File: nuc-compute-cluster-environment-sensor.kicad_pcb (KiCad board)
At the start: 4 copper layers, 112 parts, among them J1 USB4105-GF-A, J2 SM04B-SRSS-TB-LF-SN, J3 SM04B-SRSS-TB-LF-SN, U1 FT4232H-56Q, U2 AP7370-33SA-7, U3 STM32G474CET6, U4 MB85RC1MTPNF-G, U5 SHT45, U6 BME280, Y1 ABM3B-12.000MHZ-B2-T, Y2 ECS-_327-12_5-34B-TR, Y3 ABM3B-8.000MHZ-10-1-U-T

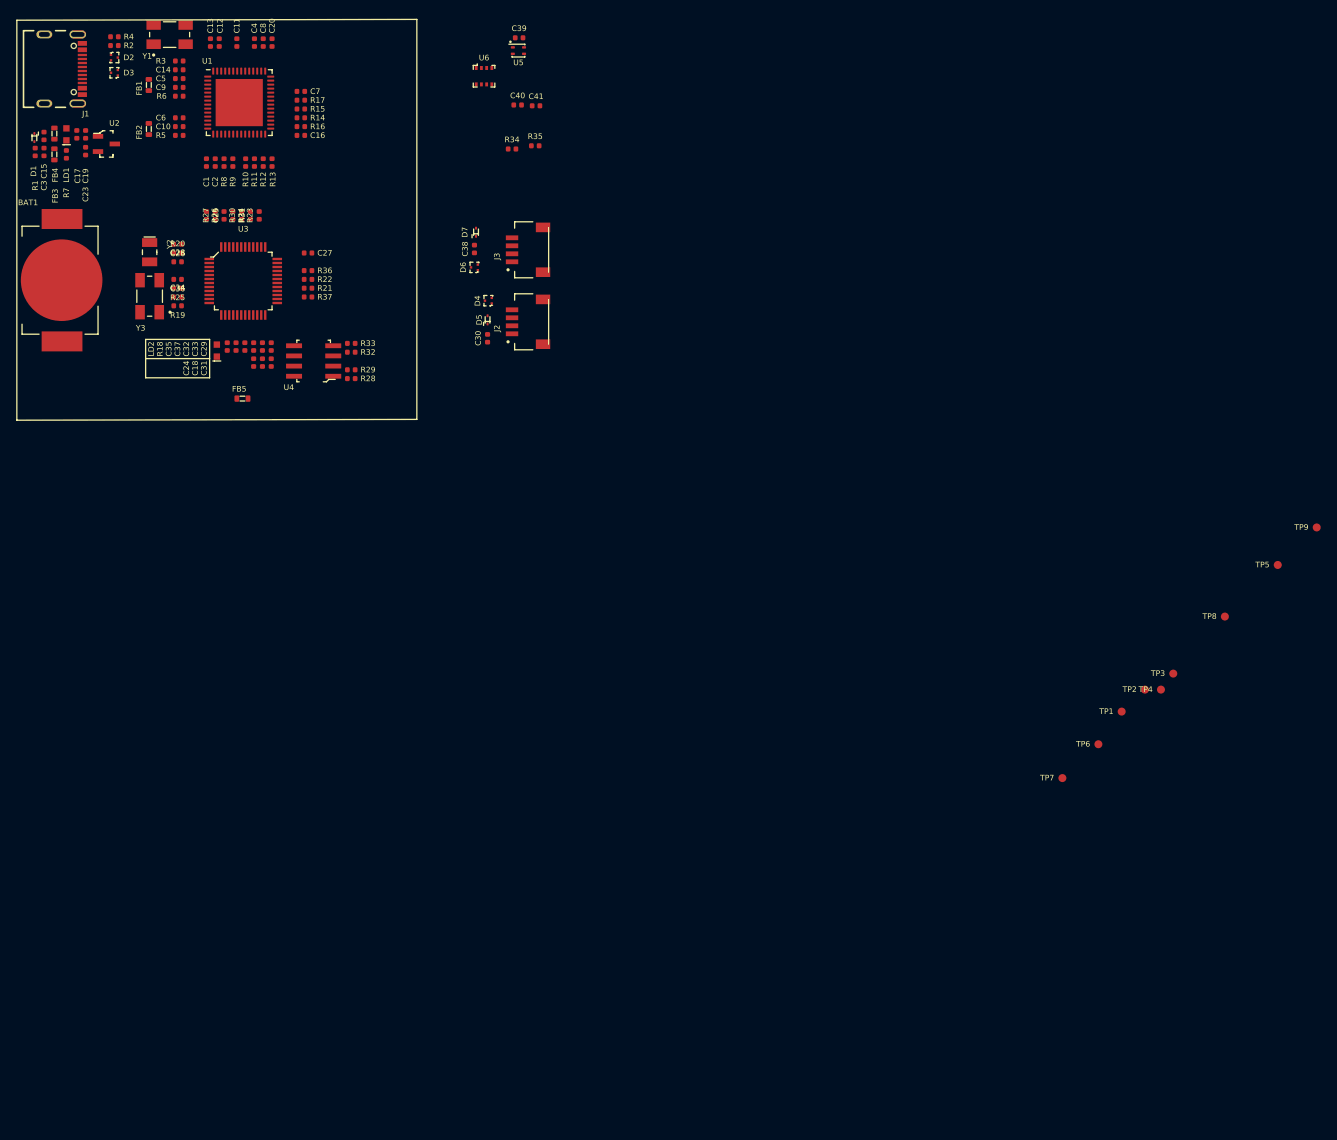
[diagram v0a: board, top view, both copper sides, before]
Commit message: Started to route signals to closest passive components to seek for possible placement optimization
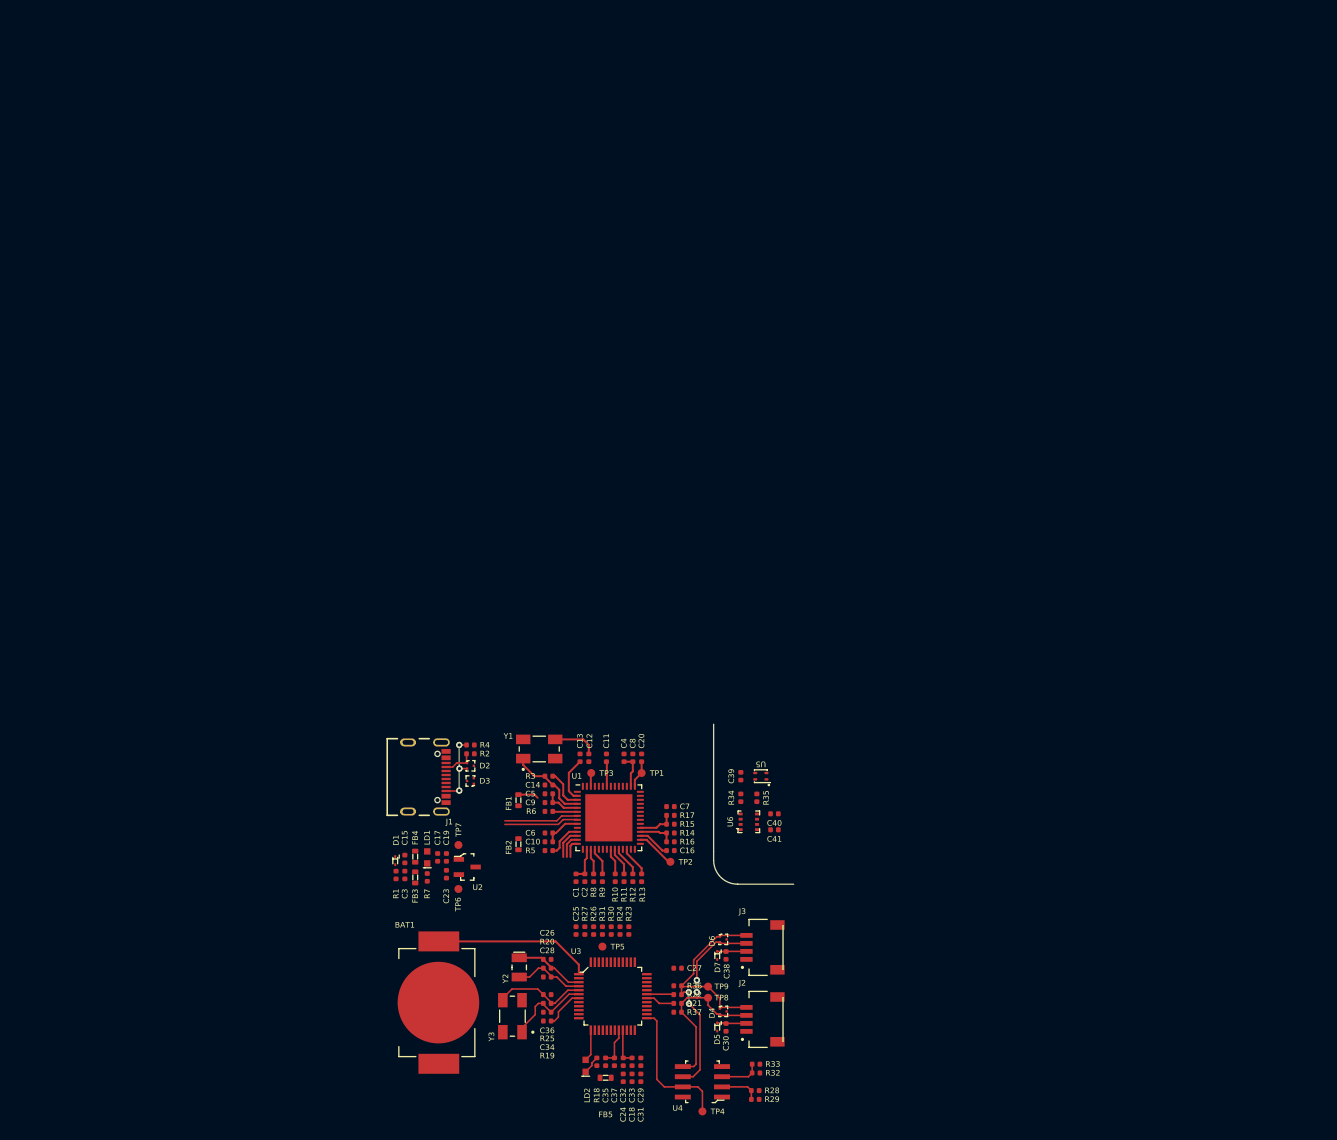
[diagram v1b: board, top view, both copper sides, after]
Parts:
- moved R29 104.2 mm to (115.3, 147.9)
- moved R32 103.3 mm to (115.4, 144.6)
- moved R33 103.3 mm to (115.4, 143.5)
- moved U4 102.4 mm to (108.7, 145.7)
- moved R28 102.3 mm to (115.3, 146.8)
- moved BAT1 101.8 mm to (75.7, 135.8)
- moved C17 101.0 mm to (75.6, 117.7)
- moved C19 101.0 mm to (76.7, 117.7)
- moved FB3 101.0 mm to (72.8, 120.2)
- moved FB4 101.0 mm to (72.8, 117.6)
- moved LD1 101.0 mm to (74.3, 117.7)
- moved R7 101.0 mm to (74.3, 120.2)
- moved C15 101.0 mm to (71.5, 117.8)
- moved C23 101.0 mm to (76.7, 119.8)
- moved C3 101.0 mm to (71.5, 119.8)
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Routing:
- net I2C_1_SCL: track 0.00 -> 36.8 mm, vias 0 -> 2
- net I2C_1_SDA: track 0.00 -> 31.8 mm, vias 0 -> 2
- net Net-(BAT1-PadP): track 0.00 -> 19.9 mm
- net +3V3: track 0.00 -> 19.0 mm
- net /FRAM_WP: track 0.00 -> 17.5 mm
- net /FTDI_+1V8: track 0.00 -> 13.0 mm
- net Net-(C36-Pad2): track 0.00 -> 11.7 mm
- net Net-(C34-Pad2): track 0.00 -> 11.0 mm
- net Net-(C12-Pad2): track 0.00 -> 10.7 mm
- net Net-(C14-Pad2): track 0.00 -> 10.3 mm
- net /USB_D_N: track 0.00 -> 9.32 mm
- net /USB_D_P: track 0.00 -> 9.32 mm
- net /USB_CC2: track 0.00 -> 9.25 mm, vias 0 -> 3
- net Net-(C28-Pad2): track 0.00 -> 8.92 mm
- net Net-(C26-Pad2): track 0.00 -> 8.79 mm
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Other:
- board outline added: 10 x 20 mm

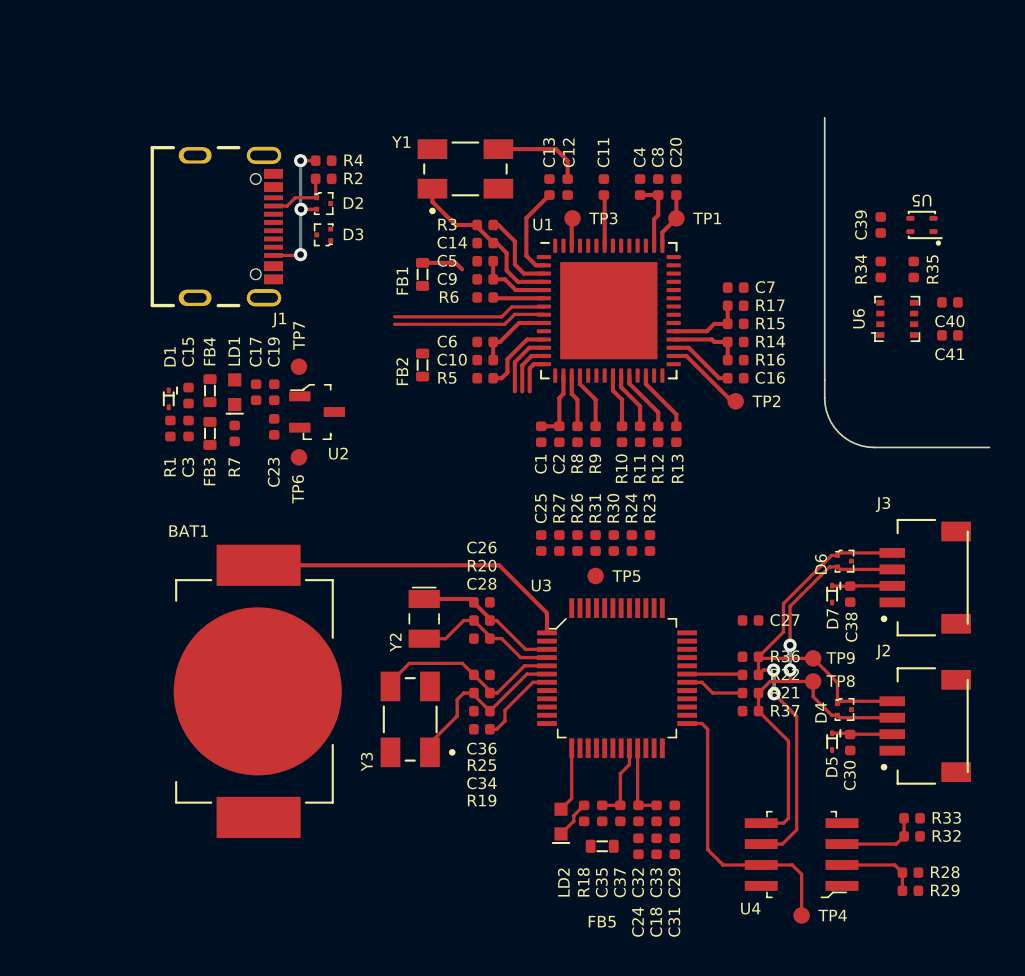
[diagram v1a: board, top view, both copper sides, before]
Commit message: Another iteration of component placements, initial routing of signals
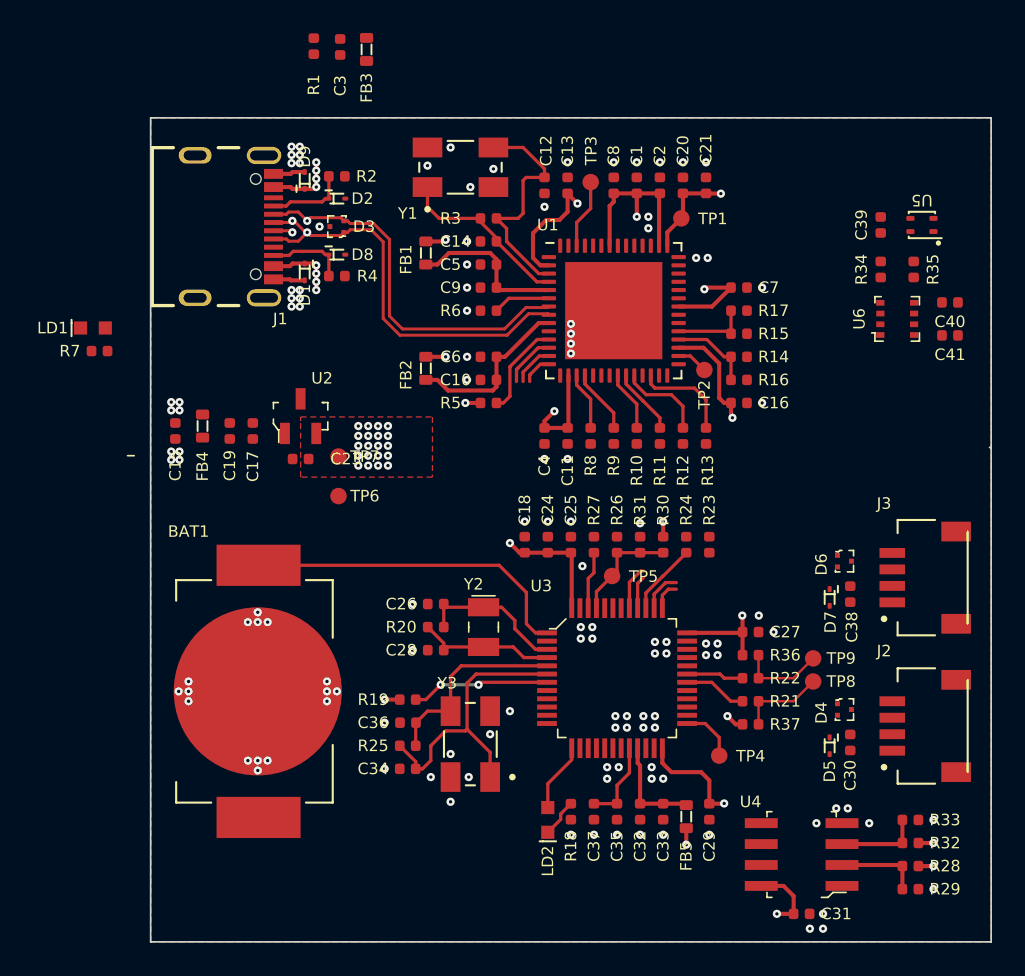
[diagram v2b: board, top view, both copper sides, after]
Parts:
- added C21: C_4u7_0402, antmicro-footprints:0402-cap, F.Cu at (102.9, 105.1)
- added D8: ESD9X5.0ST5G, antmicro-footprints:SOD-923, F.Cu at (80.5, 109.3)
- added D9: ESD9X5.0ST5G, antmicro-footprints:SOD-923, F.Cu at (78.5, 104.8)
- D2: value TPD2E009 -> ESD9X5.0ST5G; footprint antmicro-footprints:SOT-723 -> antmicro-footprints:SOD-923
- moved FB3 25.2 mm to (82.3, 96.8)
- moved C3 24.9 mm to (80.7, 96.7)
- moved R1 24.8 mm to (79.1, 96.7)
- moved C18 20.0 mm to (91.9, 126.9)
- moved C24 19.1 mm to (93.3, 126.9)
- moved C2 16.3 mm to (100.1, 105.1), turned to 90 degrees
- moved C1 16.2 mm to (98.7, 105.1), turned to 90 degrees
- moved C4 16.2 mm to (93.1, 120.3), turned to -90 degrees
- moved C11 15.3 mm to (94.5, 120.3), turned to -90 degrees
- moved D1 11.3 mm to (78.5, 110.3)
- moved TP4 10.9 mm to (103.7, 139.7)
- moved R7 9.60 mm to (66.1, 115.2), turned to 180 degrees
- moved LD1 9.44 mm to (65.7, 113.8), turned to 0 degrees
- moved C31 8.72 mm to (108.7, 149.3), turned to 180 degrees
- moved TP7 8.21 mm to (80.6, 124.0)
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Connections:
- D2 pad 2: /USB_CC2 -> GND
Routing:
- net +3V3: track 19.0 -> 54.9 mm, vias 0 -> 36
- net I2C_1_SCL: track 36.8 -> 5.21 mm, vias 2 -> 0
- net I2C_1_SDA: track 31.8 -> 5.21 mm, vias 2 -> 0
- net /USB_D_P: track 9.32 -> 25.5 mm, vias 0 -> 2
- net /USB_D_N: track 9.32 -> 25.5 mm, vias 0 -> 2
- net /FRAM_WP: track 17.5 -> 3.40 mm
- net /VBUS: track 0.00 -> 8.39 mm, vias 0 -> 12
- net Net-(C34-Pad2): track 11.0 -> 17.8 mm
- net /FTDI_+1V8: track 13.0 -> 19.9 mm, vias 0 -> 3
- net Net-(R26-Pad1): track 0.00 -> 6.68 mm
- net /FTDI_VPLL: track 4.65 -> 10.5 mm
- net /USB_CC2: track 9.25 -> 4.83 mm, vias 3 -> 0
- net Net-(R23-Pad2): track 0.00 -> 4.39 mm
- net GND: track 0.00 -> 3.86 mm, vias 0 -> 120
- net Net-(C12-Pad2): track 10.7 -> 14.3 mm
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- added copper zone on F.Cu, net +3V3
- added copper zone on In2.Cu, net +3V3
- added copper zone on In2.Cu, net /FTDI_+1V8
- added copper zone on In2.Cu, net /VBUS
- added copper zone on B.Cu, net GND
- added copper zone on F.Cu, net GND
- added copper zone on In1.Cu, net GND
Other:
- board size 10 x 20 mm -> 51 x 50 mm

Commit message: Added mounting holes and changed PCB size to 50x30mm
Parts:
- added MP1: PCB_Mount_Hole_2.7mm_M2.5_pad, antmicro-footprints:mounting-hole-2.7mm-M2.5-Pad, F.Cu at (164.0, 114.0)
- added MP2: PCB_Mount_Hole_2.7mm_M2.5_pad, antmicro-footprints:mounting-hole-2.7mm-M2.5-Pad, F.Cu at (164.0, 136.0)
- added MP3: PCB_Mount_Hole_2.7mm_M2.5_pad, antmicro-footprints:mounting-hole-2.7mm-M2.5-Pad, F.Cu at (194.0, 114.0)
- added MP4: PCB_Mount_Hole_2.7mm_M2.5_pad, antmicro-footprints:mounting-hole-2.7mm-M2.5-Pad, F.Cu at (200.0, 136.0)
- moved C27 166.0 mm to (271.1, 145.2)
- moved C29 166.0 mm to (268.6, 156.1)
- moved C37 166.0 mm to (261.6, 156.1)
- moved R21 166.0 mm to (271.1, 149.4)
- moved R22 166.0 mm to (271.1, 148.0)
- moved R23 166.0 mm to (268.6, 139.9)
- moved R27 166.0 mm to (261.6, 139.9)
- moved R36 166.0 mm to (271.1, 146.6)
- moved R37 166.0 mm to (271.1, 150.8)
- moved C24 166.0 mm to (258.8, 139.9)
- moved C25 166.0 mm to (260.2, 139.9)
- moved C26 166.0 mm to (252.0, 143.5)
- moved C28 166.0 mm to (252.0, 146.3)
- moved C33 166.0 mm to (265.8, 156.1)
- moved C34 166.0 mm to (250.3, 153.5)
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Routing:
- net Net-(BAT1-PadP): track 20.3 -> 0.70 mm
- net /USB_D_N: track 25.5 -> 7.62 mm
- net /USB_D_P: track 25.5 -> 7.62 mm
- net GND: vias 120 -> 102
- removed copper zone on F.Cu, net +3V3
- removed copper zone on In2.Cu, net +3V3
- removed copper zone on In2.Cu, net /FTDI_+1V8
- removed copper zone on In2.Cu, net /VBUS
- removed copper zone on B.Cu, net GND
- removed copper zone on F.Cu, net GND
- removed copper zone on In1.Cu, net GND
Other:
- board size 51 x 50 mm -> 50 x 30 mm

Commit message: New component placement, FTDI and related passive components moved to bottom layer
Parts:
- BAT1, C1, C10, C11, C12, C13, C14, C16, C2, C20, C21, C30, C38, C4, C5, C6, C7, C8, C9, D4, D5, D6, D7, FB1, FB2, J2, J3, R10, R11, R12, R13, R14, R15, R16, R17, R3, R5, R6, R8, R9, TP1, TP2, TP3, U1, Y1: moved to B.Cu
- moved C21 95.9 mm to (183.7, 136.4), turned to -90 degrees
- moved C20 95.7 mm to (182.6, 136.4), turned to -90 degrees
- moved C2 95.5 mm to (181.5, 136.4), turned to -90 degrees
- moved C1 95.3 mm to (180.4, 136.4), turned to -90 degrees
- moved C8 95.1 mm to (179.3, 136.4), turned to -90 degrees
- moved C14 95.0 mm to (167.8, 136.3), turned to 90 degrees
- moved Y1 94.9 mm to (171.9, 136.5), turned to -90 degrees
- moved TP3 94.6 mm to (177.2, 134.9), turned to 90 degrees
- moved C13 94.1 mm to (178.2, 136.4), turned to -90 degrees
- moved C12 93.9 mm to (177.1, 136.4)
- moved TP1 92.2 mm to (185.0, 135.9)
- moved R3 90.9 mm to (176.0, 136.4), turned to -90 degrees
- moved C5 88.2 mm to (173.1, 133.4)
- moved FB1 87.6 mm to (170.8, 133.1), turned to 0 degrees
- moved C7 86.9 mm to (186.5, 131.3)
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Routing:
- net +3V3: track 54.9 -> 23.6 mm, vias 36 -> 2
- net /USB_D_N: track 7.62 -> 20.1 mm, vias 2 -> 3
- net /USB_D_P: track 7.62 -> 19.5 mm, vias 2 -> 3
- net Net-(C34-Pad2): track 17.8 -> 7.36 mm
- net NRST: track 8.40 -> 0.00 mm, vias 2 -> 0
- net /FTDI_+1V8: track 19.9 -> 12.2 mm
- net Net-(C14-Pad2): track 10.7 -> 3.86 mm
- net Net-(C12-Pad2): track 14.3 -> 7.69 mm
- net Net-(R32-Pad1): track 5.09 -> 0.09 mm
- net Net-(R28-Pad1): track 5.09 -> 0.09 mm
- net I2C_1_SDA: track 5.21 -> 1.10 mm
- net I2C_1_SCL: track 5.21 -> 1.10 mm
- net /FTDI_VPLL: track 10.5 -> 6.39 mm
- net GND: track 3.86 -> 0.46 mm, vias 102 -> 1
- net /FRAM_WP: track 3.40 -> 0.00 mm
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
